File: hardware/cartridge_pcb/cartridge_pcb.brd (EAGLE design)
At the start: 80 x 80 mm, 88 parts, among them IC1 LM1117MPX-ADJ, Q1 2N7002, Q2 2N7002, Q3 2N7002, Q4 2N7002, Q5 2N7002, U1 MCP23017-E/SO, U2 ADS1015IDGST, U3 MCP23017-E/SO, U4 TXB0108PWR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

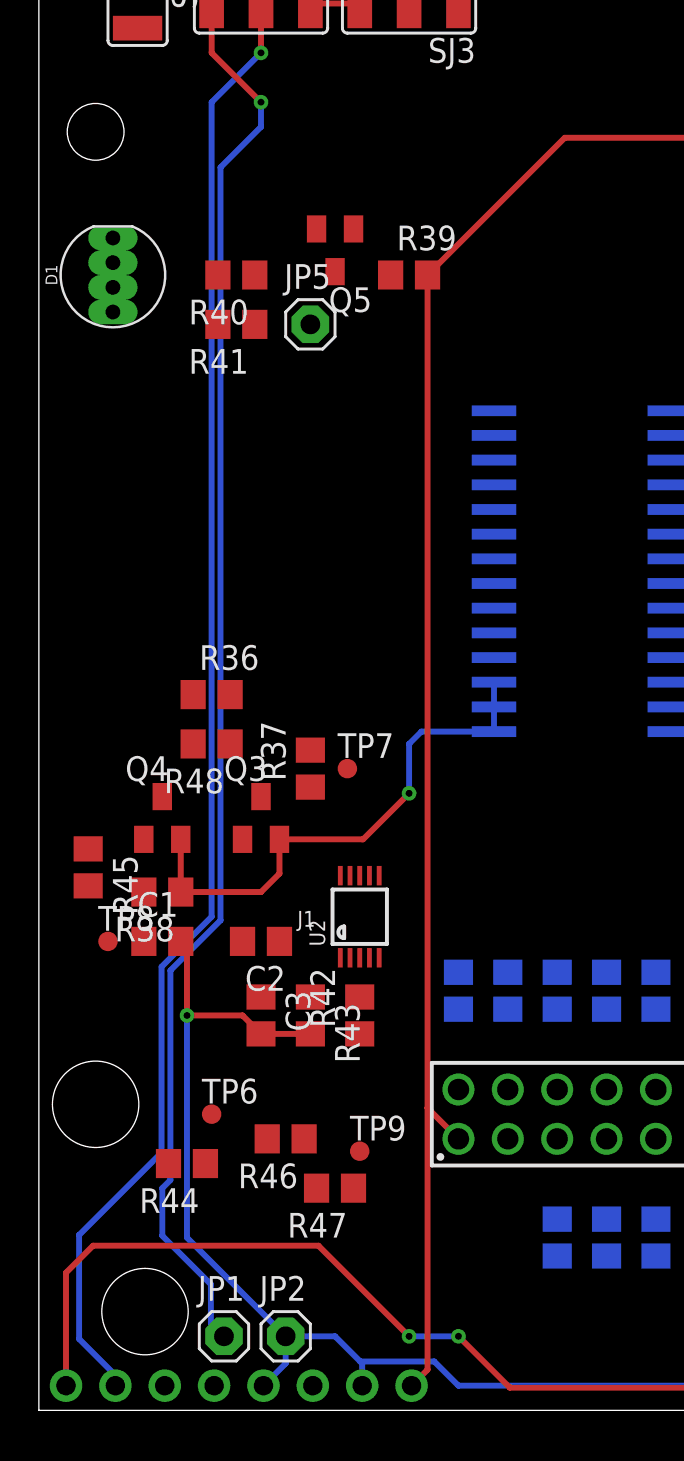
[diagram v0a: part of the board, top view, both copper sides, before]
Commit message: fix some issues of the cartridge pcb
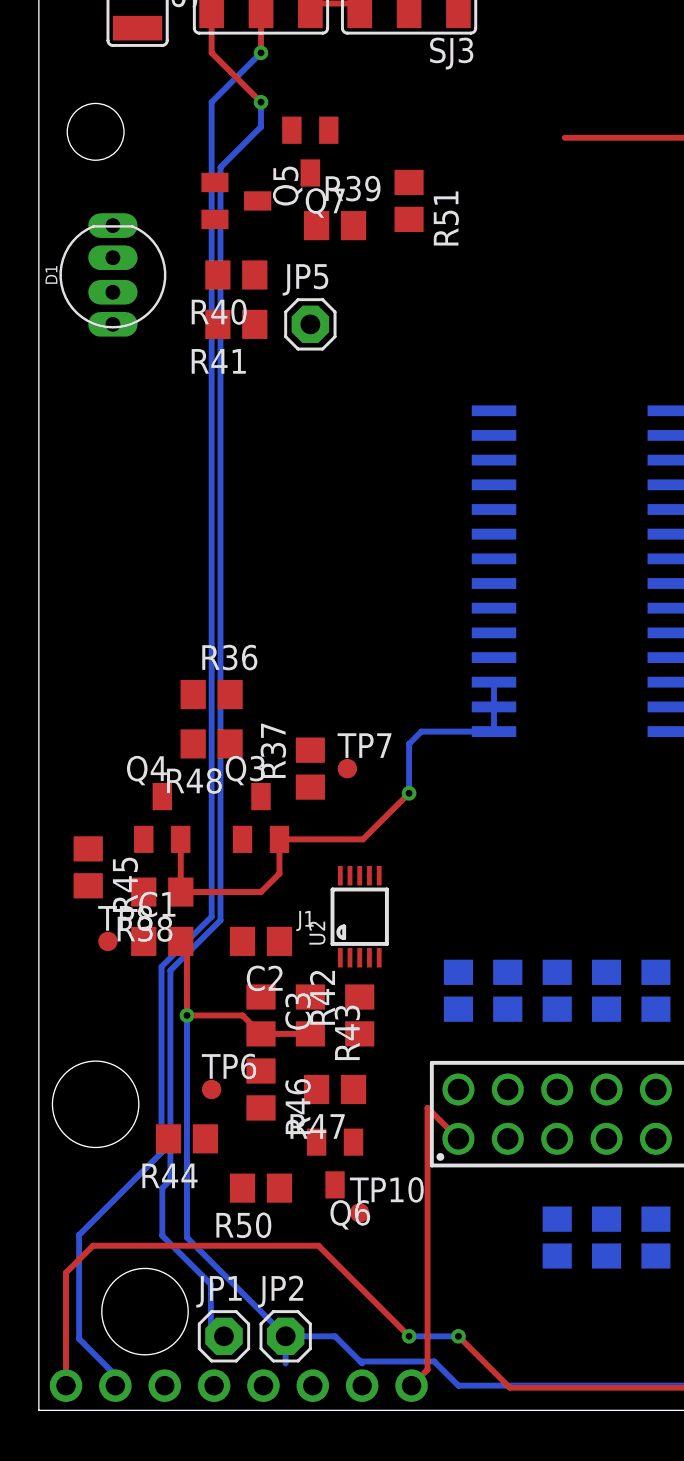
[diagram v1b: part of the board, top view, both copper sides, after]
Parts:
- removed TP9: PTR1TP10R, testpad:TP10R
- added Q6, Q7: 2N7002, transistors_gaui:SOT23
- added R50: 100K, rcl:R0805
- added R51: 10K, rcl:R0805
- added TP10: PTR1TP10R, testpad:TP10R
- moved Q5 5.68 mm to (10.2, 62.2), turned to 270 degrees
- moved R47 5.08 mm to (15.2, 16.5)
- moved R39 4.58 mm to (15.2, 61.0)
- moved R46 2.84 mm to (11.4, 16.5), turned to 270 degrees
- moved R44 1.27 mm to (7.62, 14.0)
- moved TP6 1.27 mm to (8.89, 16.5)
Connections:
- removed net N$29: JP3.1, U$1.1
- new net SHUTDOWN_OLD: Q6.1, R47.1, SJ4.2
- net +5V: now also R51.2, U1.18, U1.9, U3.15, U3.16, U3.17, U3.18, U3.9
- net GND: now also Q6.2, Q7.2
- net LIPO: now also R50.2
- net N$47: now also Q7.3, R51.1; no longer JP3.3
- net N$57: now also JP3.6, Q7.1; no longer U1.18, U1.9, U3.15, U3.16, U3.17, U3.18, U3.9
- net N$83: now also JP3.1, U$1.1
- net SHUTDOWN: now also Q6.3, R50.1, TP10.TP; no longer R47.1, SJ4.2, TP9.TP
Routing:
- net N$83: track 0.00 -> 114.8 mm, vias 0 -> 3
- net N$29: track 114.8 -> 0.00 mm, vias 3 -> 0
- net +5V: track 80.6 -> 27.7 mm
- net GND: track 241.8 -> 239.1 mm

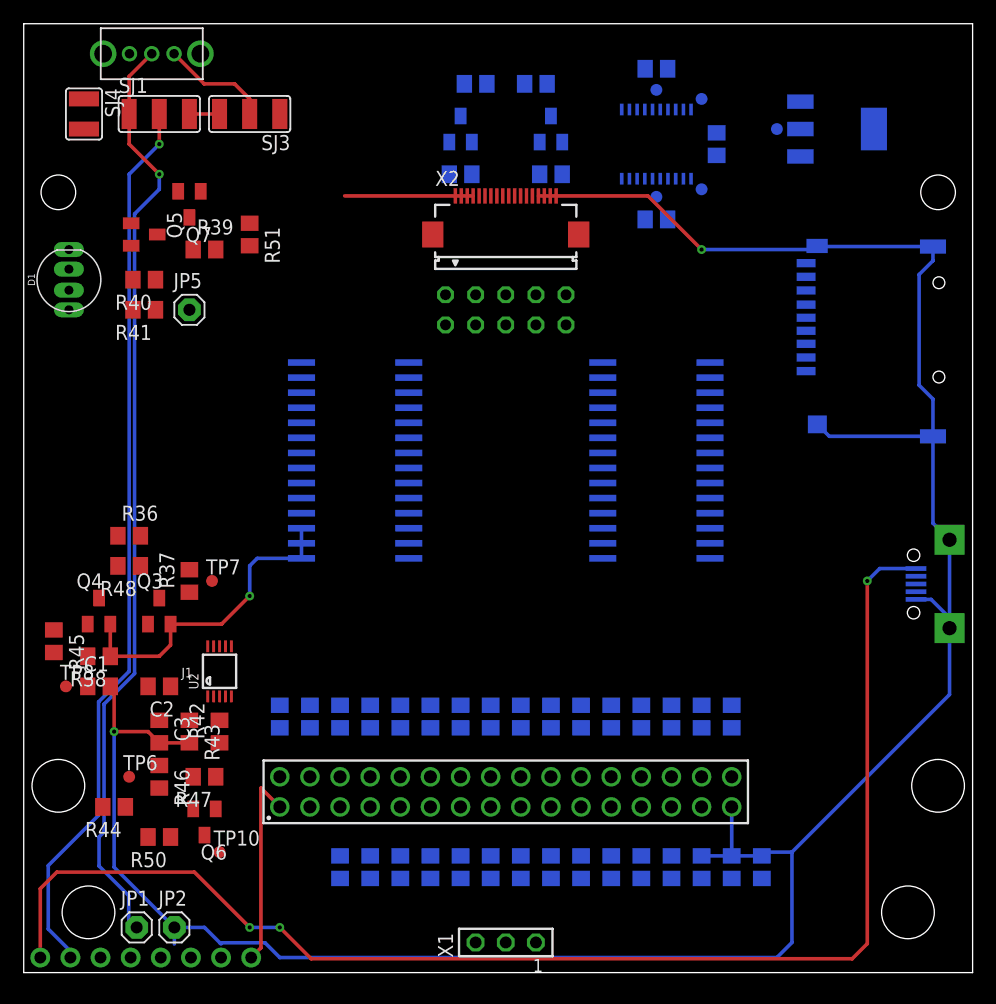
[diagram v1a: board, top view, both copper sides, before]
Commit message: fix more errors in cartridge pcb which were found while testing the cartridge reader
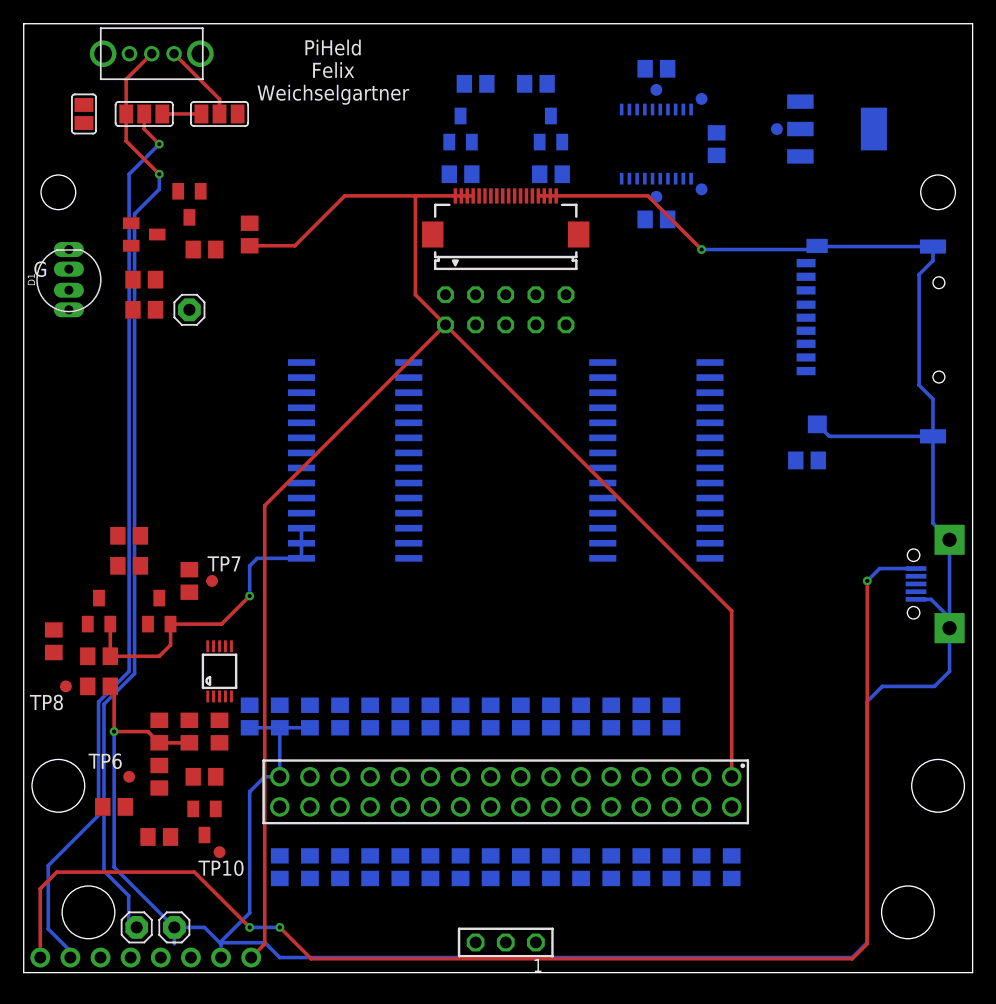
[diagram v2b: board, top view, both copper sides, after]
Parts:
- removed SJ4: (no value), jumper:SJW
- added SJ2: (no value), jumper:SJ_2
- SJ1: device jumper:SJ_2W -> jumper:SJ
- SJ3: device jumper:SJ_2W -> jumper:SJ_2
- moved C2 57.8 mm to (66.0, 43.2), flipped to the bottom
- moved R32 45.0 mm to (19.1, 21.6), turned to 270 degrees
- moved R23 40.2 mm to (59.7, 8.89), turned to 90 degrees
- moved R31 40.2 mm to (21.6, 21.6), turned to 270 degrees
- moved R8 40.2 mm to (21.6, 8.89), turned to 90 degrees
- moved R22 35.4 mm to (57.1, 8.89), turned to 90 degrees
- moved R30 35.4 mm to (24.1, 21.6), turned to 270 degrees
- moved R9 35.4 mm to (24.1, 8.89), turned to 90 degrees
- moved R10 30.7 mm to (26.7, 8.89), turned to 90 degrees
- moved R21 30.7 mm to (54.6, 8.89), turned to 90 degrees
- moved R29 30.7 mm to (54.6, 21.6), turned to 270 degrees
- moved R33 30.7 mm to (26.7, 21.6), turned to 270 degrees
- moved R11 26.2 mm to (29.2, 8.89), turned to 90 degrees
- moved R20 26.2 mm to (52.1, 8.89), turned to 90 degrees
- moved R28 26.2 mm to (52.1, 21.6), turned to 270 degrees
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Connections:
- net LIPO: now also SJ3.1; no longer SJ1.1
- net N$66: now also SJ2.1; no longer SJ3.1
- net N$79: now also SJ2.2; no longer SJ3.2
- net N$80: now also SJ1.1; no longer SJ4.1
- net N$81: now also SJ3.2; no longer SJ1.2
- net N$82: now also SJ2.3; no longer SJ1.3
- net SHUTDOWN_OLD: now also SJ1.2; no longer SJ4.2
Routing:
- net +5V: track 27.7 -> 140.7 mm
- net GND: track 239.1 -> 261.1 mm
- net N$79: track 9.22 -> 6.67 mm
- net N$82: track 2.54 -> 3.30 mm
- net N$81: track 75.8 -> 76.3 mm
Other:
- board text added: "G"
- board text added: "PiHeld Felix Weichselgartner"

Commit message: fixed error in cpcb
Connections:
- removed net VCC: R33.1
- net +5V: now also R33.1
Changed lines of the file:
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@@
 <wire x1="13.02" y1="65.87" x2="3.81" y2="59.309" width="0" layer="19" extent="1-1"/>
-</signal>
-<signal name="VCC">
-<contactref element="R33" pad="1"/>
 </signal>
 <signal name="N$2">
@@
 <wire x1="19.177" y1="1.27" x2="20.32" y2="2.413" width="0.3048" layer="1"/>
 <wire x1="20.32" y1="2.413" x2="20.32" y2="39.37" width="0.3048" layer="1"/>
+<contactref element="R33" pad="1"/>
 <wire x1="55.615" y1="72.7678" x2="65.481" y2="73.431" width="0" layer="19" extent="16-16"/>
 <wire x1="54.29" y1="76.2" x2="55.615" y2="72.7678" width="0" layer="19" extent="16-16"/>
@@
 <wire x1="32.4612" y1="41.275" x2="35.56" y2="54.61" width="0" layer="19" extent="16-16"/>
 <wire x1="23.4188" y1="38.735" x2="32.4612" y2="41.275" width="0" layer="19" extent="16-16"/>
+<wire x1="26.67" y1="22.54" x2="23.4188" y2="38.735" width="0" layer="19" extent="16-16"/>
 <wire x1="48.8188" y1="38.735" x2="32.4612" y2="41.275" width="0" layer="19" extent="16-16"/>
 <wire x1="48.8188" y1="37.465" x2="48.8188" y2="38.735" width="0" layer="19" extent="16-16"/>
